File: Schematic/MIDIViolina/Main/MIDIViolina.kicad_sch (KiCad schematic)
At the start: 20 parts, among them J1 Motor, J2 Motor, J3 Motor, J4 Motor, J5 Power in, J6 MSB 2, J7 Microstep Bridge, J8 MIDI I/O, J9 STEPPER OUT, Q1 IRF540N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

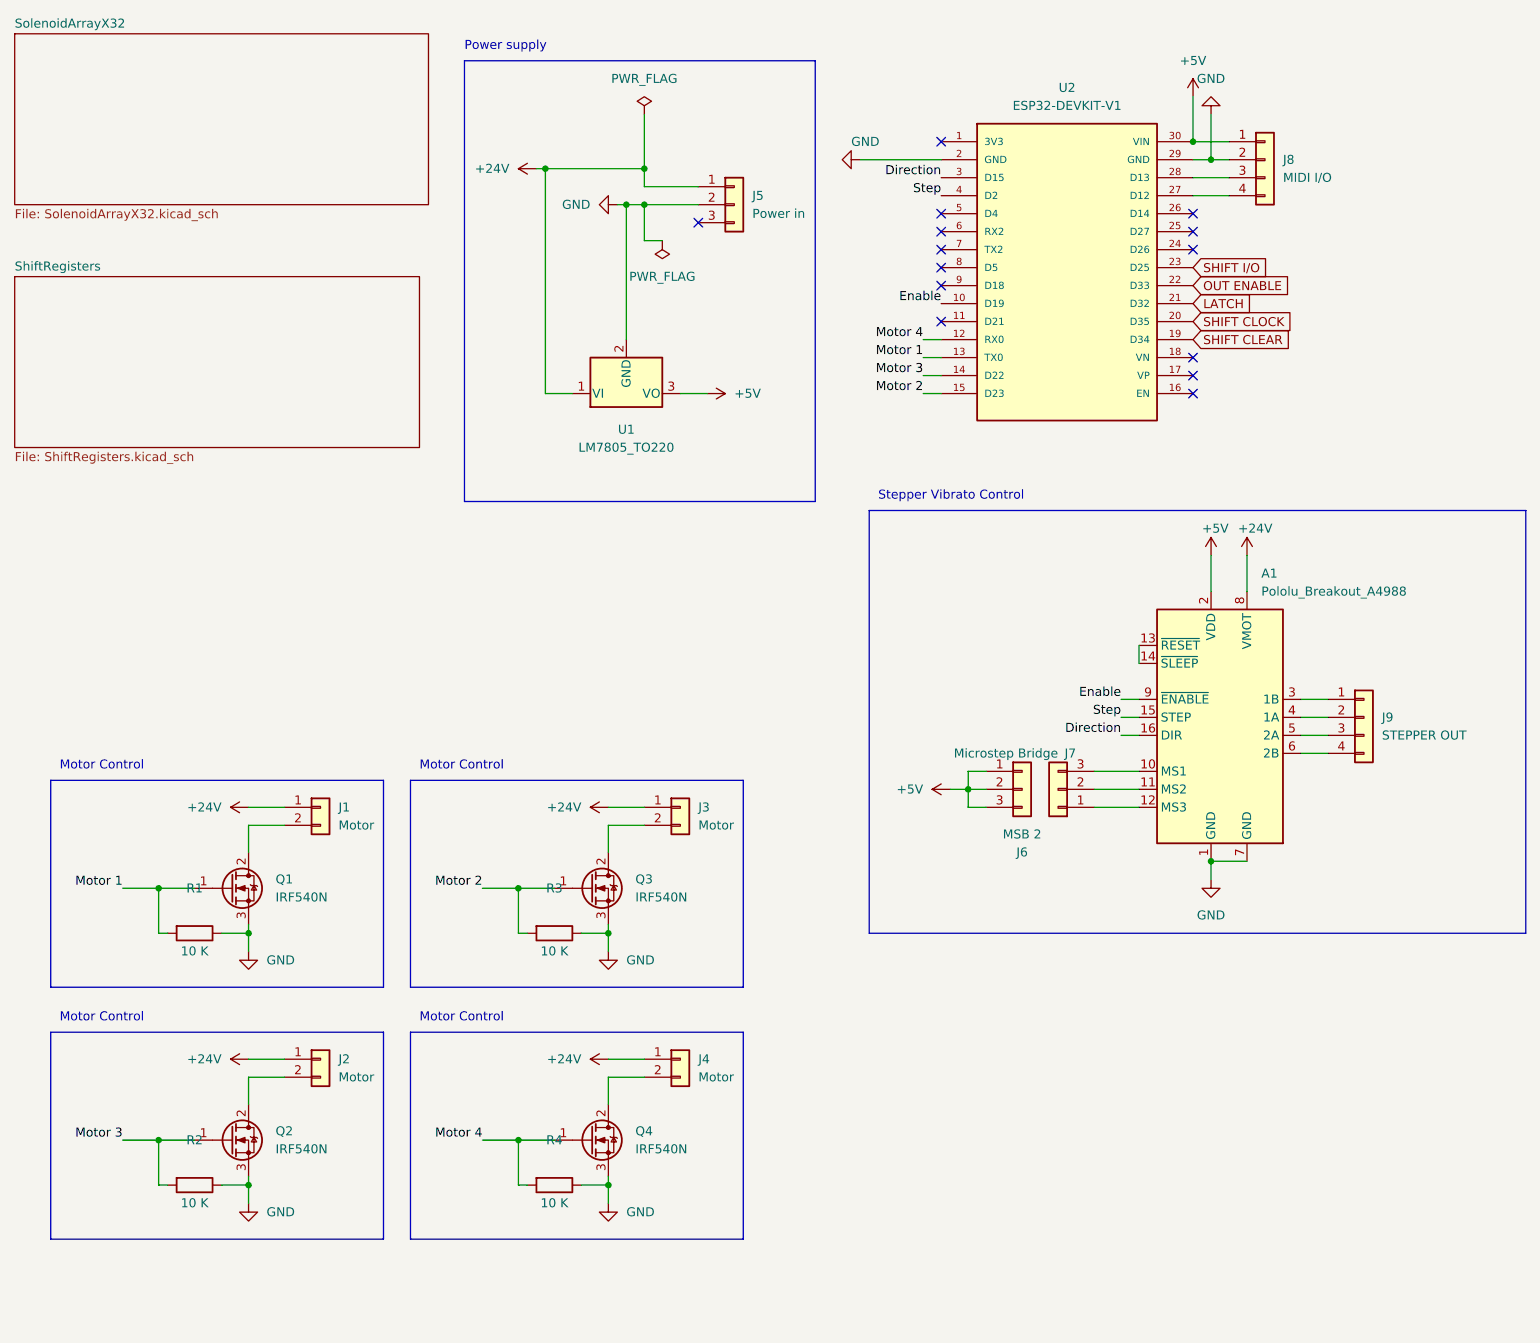
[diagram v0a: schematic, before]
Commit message: CNC Toolpaths and PCB updates
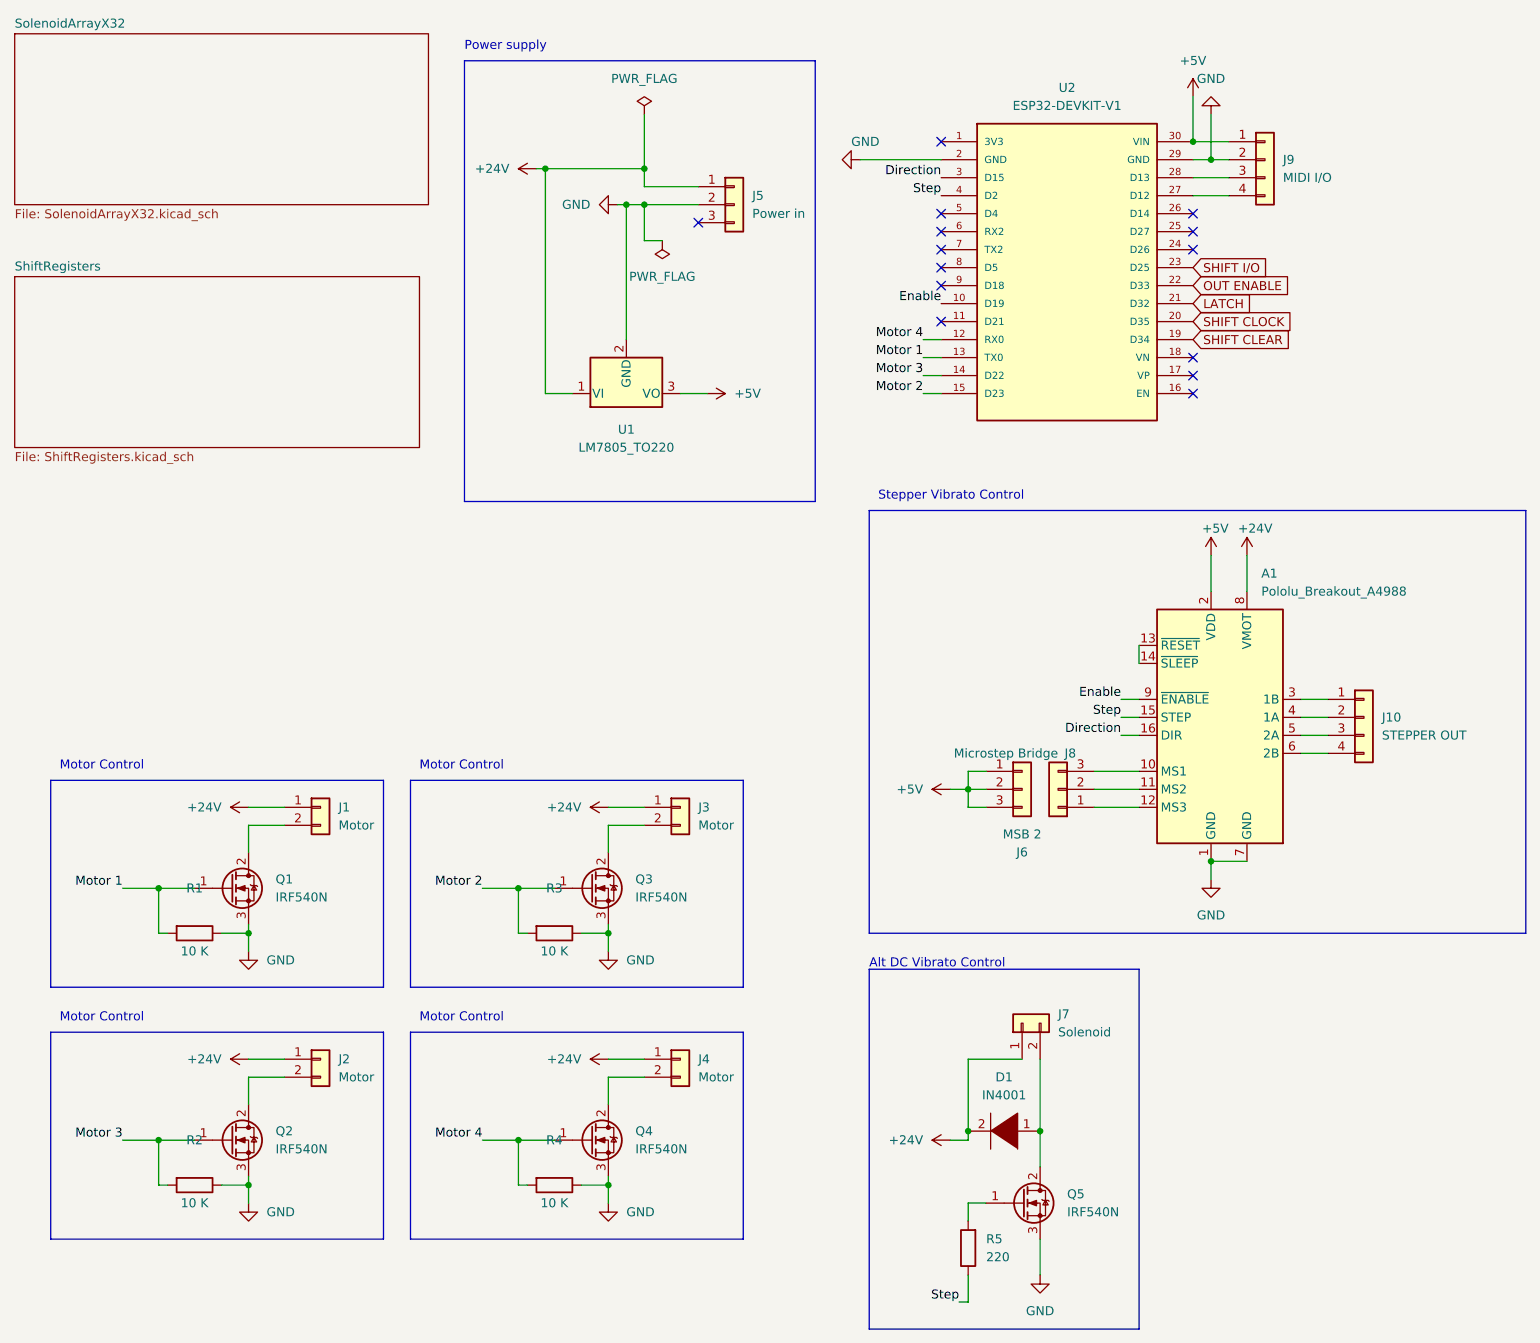
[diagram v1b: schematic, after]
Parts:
- added D1: IN4001, Diode_THT:D_DO-41_SOD81_P7.62mm_Horizontal, symbol pspice:DIODE
- added J7: Solenoid, Connector_PinHeader_2.54mm:PinHeader_1x02_P2.54mm_Vertical, symbol Connector_Generic:Conn_01x02
- added Q5: IRF540N, Package_TO_SOT_THT:TO-220-3_Vertical, symbol Transistor_FET:IRF540N
- added R5: 220, Resistor_THT:R_Axial_DIN0207_L6.3mm_D2.5mm_P7.62mm_Horizontal, symbol Device:R
- renumbered J9 to J10, J7 to J8, J8 to J9
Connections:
- net +24V: now also D1.2 (A), J7.1 (Pin_1)
- net GND: now also Q5.3 (S)
- net Step: now also R5.1
- new net: D1.1 (K), J7.2 (Pin_2), Q5.2 (D)
- new net: Q5.1 (G), R5.2
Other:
- note added: "Alt DC Vibrato Control"

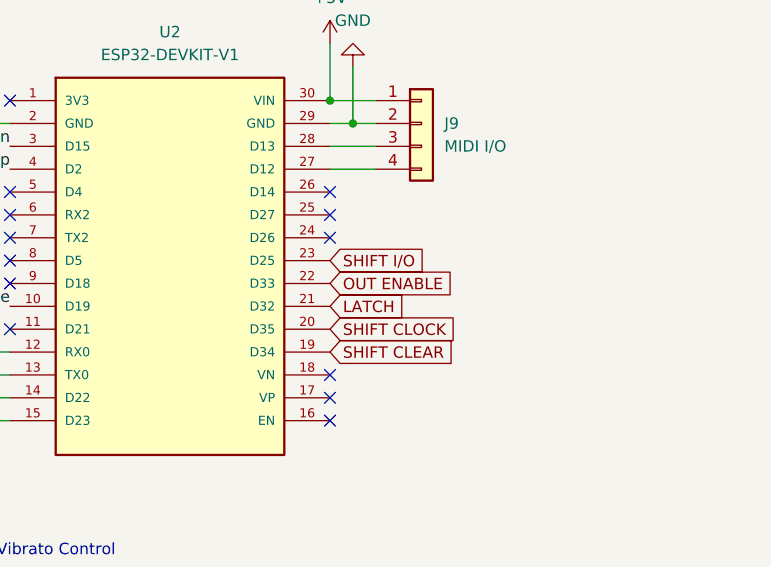
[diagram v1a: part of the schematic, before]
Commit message: some schematic updates
found a pinout error where I had them hooked up to "input only" pins. Corrected this issue.
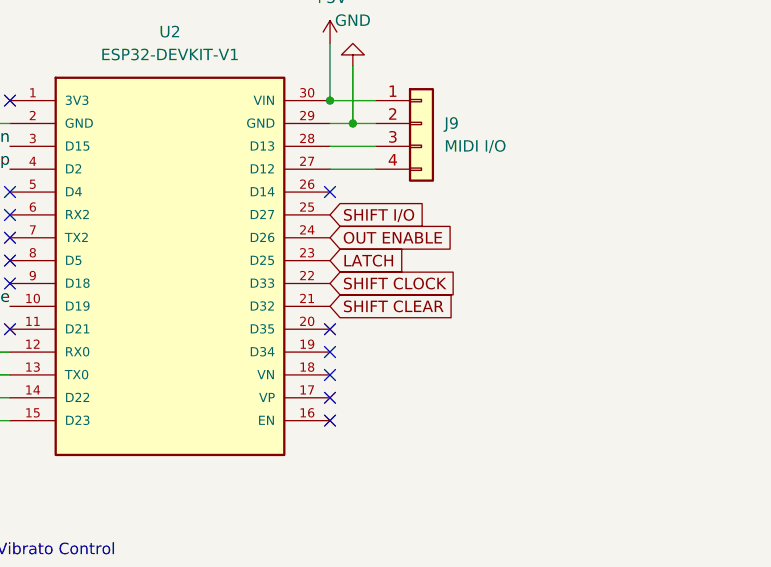
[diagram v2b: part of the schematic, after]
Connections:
- net LATCH: now also U2.23 (D25); no longer U2.21 (D32)
- net OUT ENABLE: now also U2.24 (D26); no longer U2.22 (D33)
- net SHIFT CLEAR: now also U2.21 (D32); no longer U2.19 (D34)
- net SHIFT CLOCK: now also U2.22 (D33); no longer U2.20 (D35)
- net SHIFT I/O: now also U2.25 (D27); no longer U2.23 (D25)
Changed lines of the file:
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@@
   (junction (at 36.83 172.72) (diameter 0) (color 0 0 0 0)
   )
-  (no_connect (at 182.88 46.99))
+  (no_connect (at 182.88 59.69))
   (no_connect (at 147.32 49.53))
   (no_connect (at 147.32 52.07))
@@
   (no_connect (at 182.88 64.77))
   (no_connect (at 113.03 43.18))
-  (no_connect (at 182.88 44.45))
+  (no_connect (at 182.88 57.15))
   (no_connect (at 147.32 31.75))
   (no_connect (at 147.32 44.45))
@@
     (effects (font (size 1.27 1.27)) (justify right bottom))
   )
-  (global_label "OUT ENABLE" (shape input) (at 182.88 52.07 0) (fields_autoplaced)
+  (global_label "OUT ENABLE" (shape input) (at 182.88 46.99 0) (fields_autoplaced)
     (effects (font (size 1.27 1.27)) (justify left))
-    (property "Intersheet References" "${INTERSHEET_REFS}" (id 0) (at 196.9045 51.9906 0)
+    (property "Intersheet References" "${INTERSHEET_REFS}" (id 0) (at 196.9045 46.9106 0)
       (effects (font (size 1.27 1.27)) (justify left) hide)
     )
   )
-  (global_label "SHIFT CLEAR" (shape input) (at 182.88 59.69 0) (fields_autoplaced)
+  (global_label "SHIFT CLEAR" (shape input) (at 182.88 54.61 0) (fields_autoplaced)
     (effects (font (size 1.27 1.27)) (justify left))
-    (property "Intersheet References" "${INTERSHEET_REFS}" (id 0) (at 197.2674 59.6106 0)
+    (property "Intersheet References" "${INTERSHEET_REFS}" (id 0) (at 197.2674 54.5306 0)
       (effects (font (size 1.27 1.27)) (justify left) hide)
     )
   )
-  (global_label "SHIFT I{slash}O" (shape input) (at 182.88 49.53 0) (fields_autoplaced)
+  (global_label "SHIFT I{slash}O" (shape input) (at 182.88 44.45 0) (fields_autoplaced)
     (effects (font (size 1.27 1.27)) (justify left))
-    (property "Intersheet References" "${INTERSHEET_REFS}" (id 0) (at 194.7274 49.4506 0)
+    (property "Intersheet References" "${INTERSHEET_REFS}" (id 0) (at 194.7274 44.3706 0)
       (effects (font (size 1.27 1.27)) (justify left) hide)
     )
   )
-  (global_label "SHIFT CLOCK" (shape input) (at 182.88 57.15 0) (fields_autoplaced)
+  (global_label "SHIFT CLOCK" (shape input) (at 182.88 52.07 0) (fields_autoplaced)
     (effects (font (size 1.27 1.27)) (justify left))
-    (property "Intersheet References" "${INTERSHEET_REFS}" (id 0) (at 197.6302 57.0706 0)
+    (property "Intersheet References" "${INTERSHEET_REFS}" (id 0) (at 197.6302 51.9906 0)
       (effects (font (size 1.27 1.27)) (justify left) hide)
     )
   )
-  (global_label "LATCH" (shape input) (at 182.88 54.61 0) (fields_autoplaced)
+  (global_label "LATCH" (shape input) (at 182.88 49.53 0) (fields_autoplaced)
     (effects (font (size 1.27 1.27)) (justify left))
-    (property "Intersheet References" "${INTERSHEET_REFS}" (id 0) (at 190.9779 54.5306 0)
+    (property "Intersheet References" "${INTERSHEET_REFS}" (id 0) (at 190.9779 49.4506 0)
       (effects (font (size 1.27 1.27)) (justify left) hide)
     )

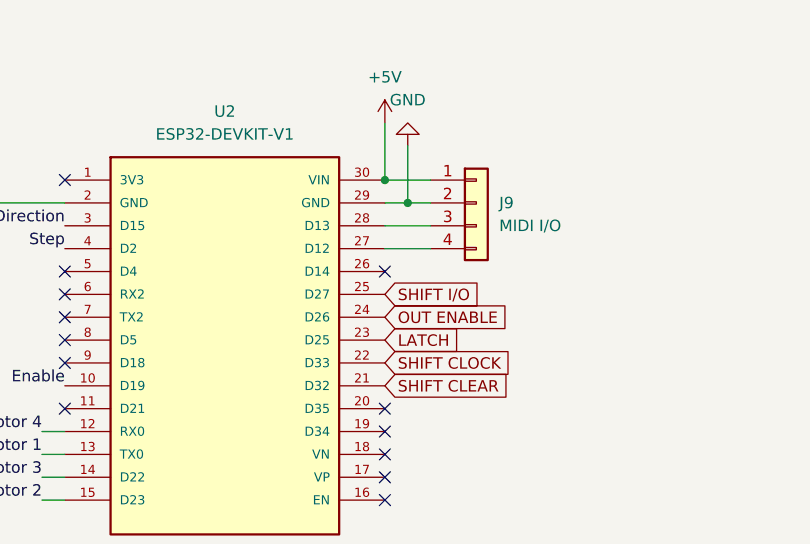
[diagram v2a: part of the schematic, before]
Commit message: fix pin routing problems
added extra thru-vias and corrected pinouts
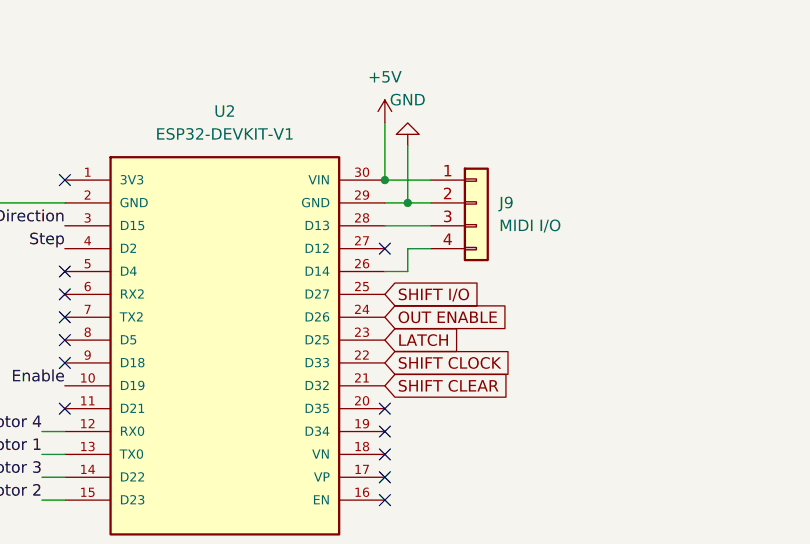
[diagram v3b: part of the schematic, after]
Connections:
- net at J9.4 (Pin_4): now also U2.26 (D14); no longer U2.27 (D12)
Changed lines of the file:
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@@
   (no_connect (at 147.32 46.99))
   (no_connect (at 182.88 67.31))
-  (no_connect (at 182.88 41.91))
+  (no_connect (at 182.88 39.37))
+  (wire (pts (xy 185.42 41.91) (xy 185.42 39.37))
+    (stroke (width 0) (type default) (color 0 0 0 0))
+  )
   (wire (pts (xy 151.13 171.45) (xy 151.13 172.72))
     (stroke (width 0) (type default) (color 0 0 0 0))
@@
     (stroke (width 0) (type default) (color 0 0 0 0))
   )
+  (wire (pts (xy 185.42 39.37) (xy 187.96 39.37))
+    (stroke (width 0) (type default) (color 0 0 0 0))
+  )
   (polyline (pts (xy 137.16 143.51) (xy 229.87 143.51))
     (stroke (width 0) (type default) (color 0 0 0 0))
@@
     (stroke (width 0) (type default) (color 0 0 0 0))
   )
+  (wire (pts (xy 182.88 41.91) (xy 185.42 41.91))
+    (stroke (width 0) (type default) (color 0 0 0 0))
+  )
   (polyline (pts (xy 72.39 121.92) (xy 119.38 121.92))
     (stroke (width 0) (type default) (color 0 0 0 0))
@@
     (stroke (width 0) (type default) (color 0 0 0 0))
   )
-  (wire (pts (xy 182.88 39.37) (xy 187.96 39.37))
-    (stroke (width 0) (type default) (color 0 0 0 0))
-  )

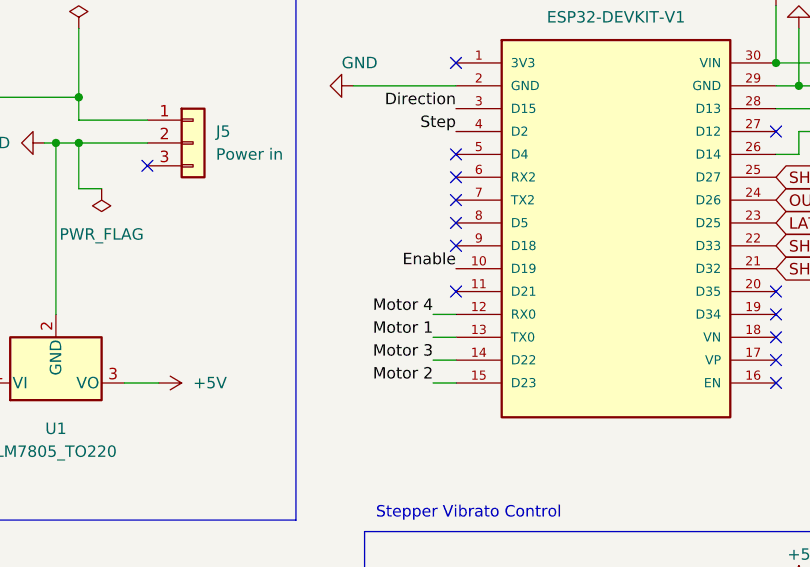
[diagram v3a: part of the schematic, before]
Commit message: update PCB and added rosen wheel
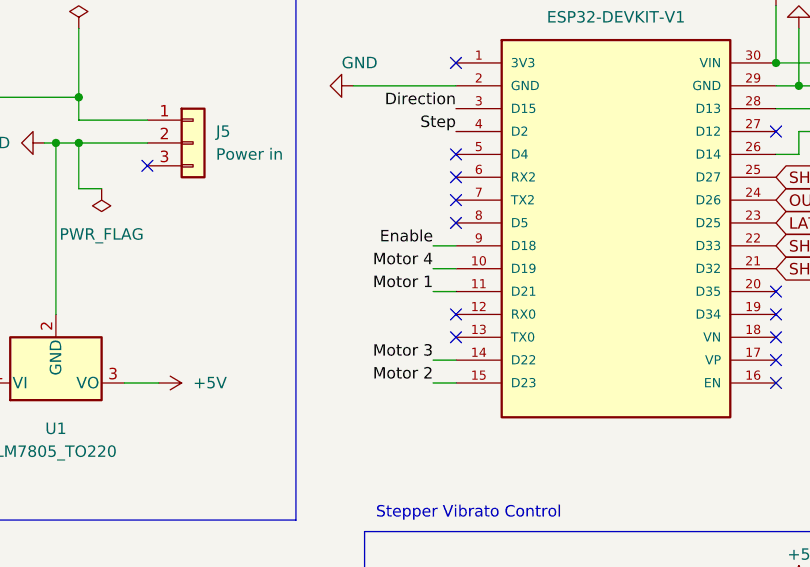
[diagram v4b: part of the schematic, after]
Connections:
- net Enable: now also U2.9 (D18); no longer U2.10 (D19)
- net Motor 1: now also U2.11 (D21); no longer U2.13 (TX0)
- net Motor 4: now also U2.10 (D19); no longer U2.12 (RX0)
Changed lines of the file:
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@@
   (no_connect (at 182.88 59.69))
   (no_connect (at 147.32 49.53))
-  (no_connect (at 147.32 52.07))
   (no_connect (at 147.32 41.91))
-  (no_connect (at 147.32 57.15))
   (no_connect (at 182.88 62.23))
   (no_connect (at 182.88 64.77))
@@
   (no_connect (at 182.88 67.31))
   (no_connect (at 182.88 39.37))
+  (no_connect (at 147.32 62.23))
+  (no_connect (at 147.32 59.69))
   (wire (pts (xy 185.42 41.91) (xy 185.42 39.37))
     (stroke (width 0) (type default) (color 0 0 0 0))
@@
     (stroke (width 0) (type default) (color 0 0 0 0))
   )
+  (wire (pts (xy 144.78 57.15) (xy 147.32 57.15))
+    (stroke (width 0) (type default) (color 0 0 0 0))
+  )
   (wire (pts (xy 100.33 132.08) (xy 100.33 128.27))
     (stroke (width 0) (type default) (color 0 0 0 0))
@@
     (stroke (width 0) (type default) (color 0 0 0 0))
   )
+  (wire (pts (xy 144.78 52.07) (xy 147.32 52.07))
+    (stroke (width 0) (type default) (color 0 0 0 0))
+  )
   (wire (pts (xy 100.33 128.27) (xy 105.41 128.27))
     (stroke (width 0) (type default) (color 0 0 0 0))
@@
     (stroke (width 0) (type default) (color 0 0 0 0))
   )
-  (wire (pts (xy 144.78 59.69) (xy 147.32 59.69))
-    (stroke (width 0) (type default) (color 0 0 0 0))
-  )
   (polyline (pts (xy 137.16 83.82) (xy 137.16 143.51))
     (stroke (width 0) (type default) (color 0 0 0 0))
@@
     (stroke (width 0) (type default) (color 0 0 0 0))
   )
-  (wire (pts (xy 144.78 62.23) (xy 147.32 62.23))
-    (stroke (width 0) (type default) (color 0 0 0 0))
-  )
   (wire (pts (xy 49.53 161.29) (xy 54.61 161.29))
     (stroke (width 0) (type default) (color 0 0 0 0))
@@
     (stroke (width 0) (type default) (color 0 0 0 0))
   )
+  (wire (pts (xy 144.78 54.61) (xy 147.32 54.61))
+    (stroke (width 0) (type default) (color 0 0 0 0))
+  )
   (wire (pts (xy 185.42 27.94) (xy 185.42 34.29))
     (stroke (width 0) (type default) (color 0 0 0 0))
@@
     (effects (font (size 1.27 1.27)) (justify left bottom))
   )
-  (label "Enable" (at 147.32 54.61 180)
+  (label "Enable" (at 144.78 52.07 180)
     (effects (font (size 1.27 1.27)) (justify right bottom))
   )
@@
     (effects (font (size 1.27 1.27)) (justify right bottom))
   )
-  (label "Motor 1" (at 144.78 62.23 180)
+  (label "Motor 1" (at 144.78 57.15 180)
     (effects (font (size 1.27 1.27)) (justify right bottom))
   )
@@
     (effects (font (size 1.27 1.27)) (justify right bottom))
   )
-  (label "Motor 4" (at 144.78 59.69 180)
-    (effects (font (size 1.27 1.27)) (justify right bottom))
-  )
+  (label "Motor 4" (at 144.78 54.61 180)
+    (effects (font (size 1.27 1.27)) (justify right bottom))
+  )
